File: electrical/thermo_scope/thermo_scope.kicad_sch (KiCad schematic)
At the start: 9 parts, among them J1 external i2c, J2 BTN, U1 PicoW, U2 Low Noise Frontend, U3 Power Supply, U4 GPS, U5 CR2013-MI2120, U6 BMP280

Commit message: Much more progress
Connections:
- net LCD_RESET: now reaches U5.4 (RESET)
- net LCD_RESET: now also U1.29 (GPIO22)
- net LCD_DC: now reaches U5.5 (D/~{C})
- net LCD_DC: now also U1.31 (GPIO26_ADC0)
- net LCD_LED: now reaches U5.8 (LED)
- net LCD_LED: now also U1.21 (GPIO16)
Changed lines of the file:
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@@
+    (stroke (width 0) (type default))
+  )
+  (wire (pts (xy 91.44 121.92) (xy 105.41 121.92))
     (stroke (width 0) (type default))
   )
@@
     (stroke (width 0) (type default))
   )
+  (wire (pts (xy 91.44 106.68) (xy 105.41 106.68))
+    (stroke (width 0) (type default))
+  )
   (wire (pts (xy 33.02 111.76) (xy 50.8 111.76))
     (stroke (width 0) (type default))
@@
     (stroke (width 0) (type default))
   )
+  (wire (pts (xy 91.44 119.38) (xy 105.41 119.38))
+    (stroke (width 0) (type default))
+  )
   (wire (pts (xy 43.18 40.64) (xy 43.18 46.99))
     (stroke (width 0) (type default))
@@
     (effects (font (size 1.27 1.27)) (justify left bottom))
   )
+  (label "LCD_LED" (at 158.75 97.79 0) (fields_autoplaced)
+    (effects (font (size 1.27 1.27)) (justify left bottom))
+  )
   (label "MAX11254_RDYB" (at 105.41 69.85 0) (fields_autoplaced)
     (effects (font (size 1.27 1.27)) (justify left bottom))
@@
     (effects (font (size 1.27 1.27)) (justify left bottom))
   )
+  (label "LCD_RESET" (at 158.75 77.47 0) (fields_autoplaced)
+    (effects (font (size 1.27 1.27)) (justify left bottom))
+  )
   (label "SPI0_SCK" (at 33.02 111.76 0) (fields_autoplaced)
     (effects (font (size 1.27 1.27)) (justify left bottom))
@@
     (effects (font (size 1.27 1.27)) (justify left bottom))
   )
+  (label "LCD_DC" (at 158.75 72.39 0) (fields_autoplaced)
+    (effects (font (size 1.27 1.27)) (justify left bottom))
+  )
   (label "SPI1_MOSI" (at 105.41 111.76 0) (fields_autoplaced)
     (effects (font (size 1.27 1.27)) (justify left bottom))
@@
     (effects (font (size 1.27 1.27)) (justify left bottom))
   )
+  (label "LCD_RESET" (at 105.41 121.92 0) (fields_autoplaced)
+    (effects (font (size 1.27 1.27)) (justify left bottom))
+  )
   (label "SPI0_SCK" (at 105.41 57.15 0) (fields_autoplaced)
     (effects (font (size 1.27 1.27)) (justify left bottom))
@@
     (effects (font (size 1.27 1.27)) (justify left bottom))
   )
+  (label "LCD_LED" (at 105.41 119.38 0) (fields_autoplaced)
+    (effects (font (size 1.27 1.27)) (justify left bottom))
+  )
   (label "I2C1_SCL" (at 158.75 87.63 0) (fields_autoplaced)
     (effects (font (size 1.27 1.27)) (justify left bottom))
@@
     (effects (font (size 1.27 1.27)) (justify left bottom))
   )
+  (label "LCD_DC" (at 105.41 106.68 0) (fields_autoplaced)
+    (effects (font (size 1.27 1.27)) (justify left bottom))
+  )

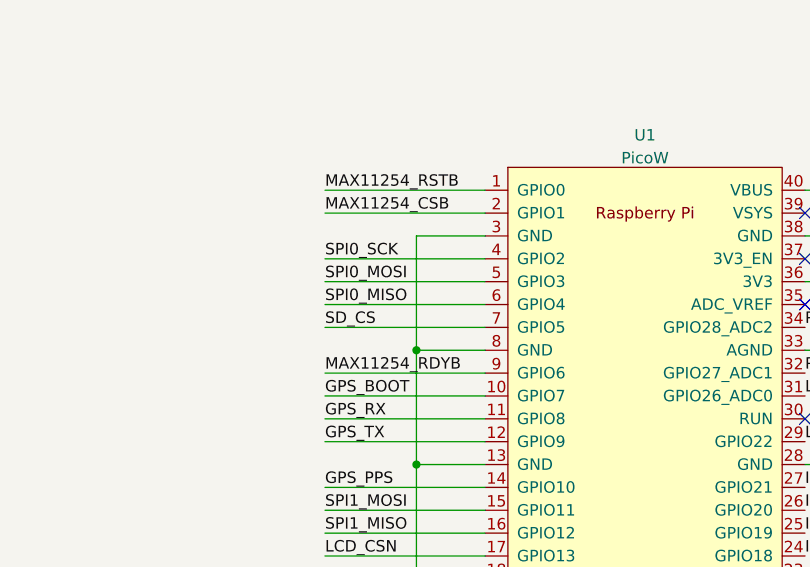
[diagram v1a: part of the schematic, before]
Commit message: Refactored to using cw_pico_library
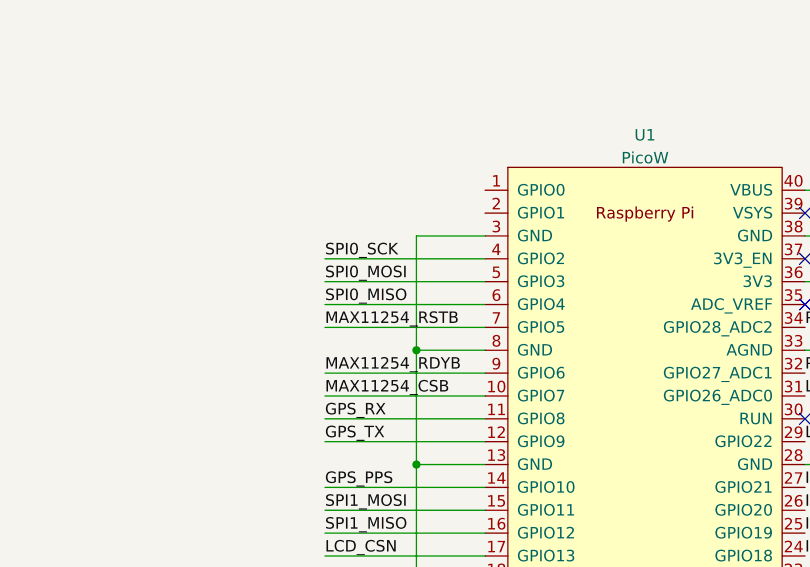
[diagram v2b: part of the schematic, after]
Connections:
- net GPS_BOOT: no longer U1.10 (GPIO7)
- net MAX11254_CSB: now also U1.10 (GPIO7); no longer U1.2 (GPIO1)
- net MAX11254_RSTB: now also U1.7 (GPIO5); no longer U1.1 (GPIO0)
- net SD_CS: no longer U1.7 (GPIO5)
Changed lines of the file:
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@@
+    (stroke (width 0) (type default))
+  )
+  (wire (pts (xy 105.41 72.39) (xy 123.19 72.39))
     (stroke (width 0) (type default))
   )
@@
     (stroke (width 0) (type default))
   )
+  (wire (pts (xy 105.41 64.77) (xy 123.19 64.77))
+    (stroke (width 0) (type default))
+  )
   (wire (pts (xy 158.75 54.61) (xy 167.64 54.61))
     (stroke (width 0) (type default))
@@
     (stroke (width 0) (type default))
   )
-  (wire (pts (xy 105.41 49.53) (xy 123.19 49.53))
-    (stroke (width 0) (type default))
-  )
   (wire (pts (xy 91.44 116.84) (xy 105.41 116.84))
     (stroke (width 0) (type default))
@@
     (stroke (width 0) (type default))
   )
-  (wire (pts (xy 105.41 64.77) (xy 123.19 64.77))
-    (stroke (width 0) (type default))
-  )
   (wire (pts (xy 190.5 135.89) (xy 200.66 135.89))
     (stroke (width 0) (type default))
@@
     (stroke (width 0) (type default))
   )
-  (wire (pts (xy 105.41 72.39) (xy 123.19 72.39))
-    (stroke (width 0) (type default))
-  )
   (wire (pts (xy 222.25 72.39) (xy 199.39 72.39))
     (stroke (width 0) (type default))
@@
     (stroke (width 0) (type default))
   )
-  (wire (pts (xy 105.41 52.07) (xy 123.19 52.07))
-    (stroke (width 0) (type default))
-  )
   (wire (pts (xy 30.48 151.13) (xy 48.26 151.13))
     (stroke (width 0) (type default))
@@
     (effects (font (size 1.27 1.27)) (justify left bottom))
   )
-  (label "MAX11254_RSTB" (at 105.41 49.53 0) (fields_autoplaced)
-    (effects (font (size 1.27 1.27)) (justify left bottom))
-  )
   (label "MAX11254_RSTB" (at 204.47 38.1 0) (fields_autoplaced)
     (effects (font (size 1.27 1.27)) (justify left bottom))
@@
     (effects (font (size 1.27 1.27)) (justify left bottom))
   )
-  (label "GPS_BOOT" (at 105.41 72.39 0) (fields_autoplaced)
-    (effects (font (size 1.27 1.27)) (justify left bottom))
-  )
-  (label "SD_CS" (at 105.41 64.77 0) (fields_autoplaced)
+  (label "MAX11254_CSB" (at 105.41 72.39 0) (fields_autoplaced)
     (effects (font (size 1.27 1.27)) (justify left bottom))
   )
@@
     (effects (font (size 1.27 1.27)) (justify left bottom))
   )
+  (label "MAX11254_RSTB" (at 105.41 64.77 0) (fields_autoplaced)
+    (effects (font (size 1.27 1.27)) (justify left bottom))
+  )
   (label "PWR_BTN" (at 166.37 27.94 0) (fields_autoplaced)
     (effects (font (size 1.27 1.27)) (justify left bottom))
@@
     (effects (font (size 1.27 1.27)) (justify left bottom))
   )
-  (label "MAX11254_CSB" (at 105.41 52.07 0) (fields_autoplaced)
-    (effects (font (size 1.27 1.27)) (justify left bottom))
-  )
